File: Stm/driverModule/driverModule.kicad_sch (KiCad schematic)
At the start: 0 parts

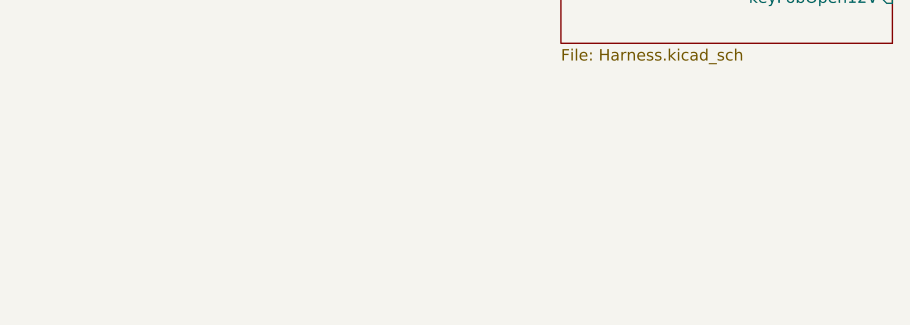
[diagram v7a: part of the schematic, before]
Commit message: libraries
Add new molex connectors
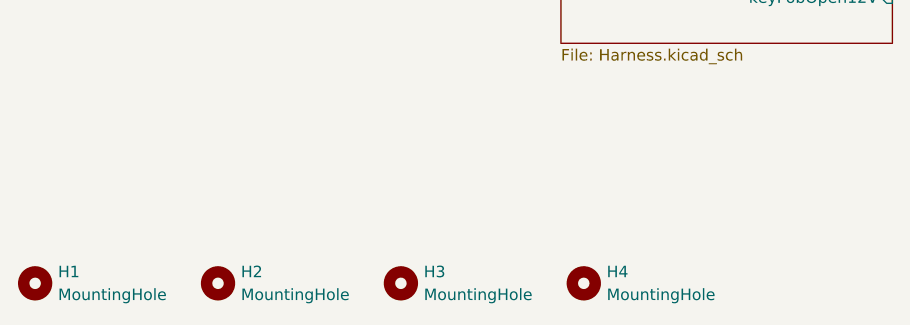
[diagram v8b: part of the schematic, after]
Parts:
- added H1, H2, H3, H4: MountingHole, MountingHole:MountingHole_2.2mm_M2, symbol Mechanical:MountingHole
